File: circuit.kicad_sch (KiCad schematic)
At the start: 9 parts, among them J1 CONN4, U1 LM358, U2 74HC00

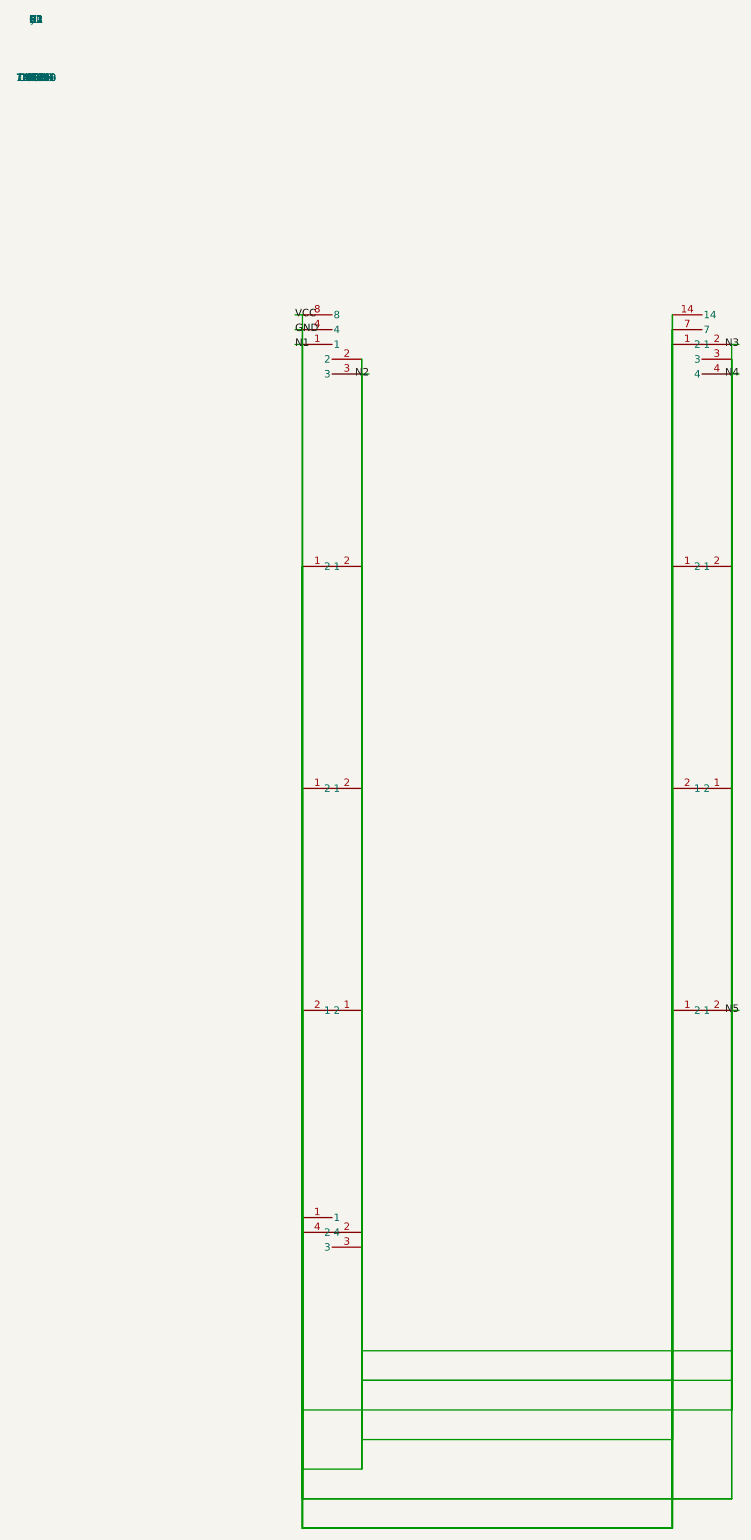
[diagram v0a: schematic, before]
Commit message: fix: v0.5.2 — KiCad pin-transform authority + net-derivation fidelity + schematic best-practice checks
Validation round: live-probed KiCad 10.0.6 itself with a 4-pin symbol
at instance rot 0 and rot 90, all four pin directions. AUTHORITATIVE
transform: a lib pin (px,py) renders at origin + R(-rot)·(px,-py) —
mirror the lib Y, then rotate by MINUS the instance rotation. The
v0.4.2 'mirror-only' inference was rot-0-only evidence; the earlier
mirror-then-rotate-by-+rot double-flipped rot-180 pins onto their
neighbors (found by the decoupling test).

NET DERIVATION FIDELITY (live-verified against kicad-cli's own netlist):
- point-on-segment connection added so labels attach anywhere along a
  wire (midpoint labels previously produced unnamed nets)
- scoped to labels/no-connects only: KiCad connects PINS to wires only
  at wire ENDPOINTS — a wire passing through a pin position is NOT a
  connection (the generated 555's long vertical drops pass near other
  pins; the unscoped test merged every net into one)
- HashMap key type bug in the decoupling check fixed (a &String key vs
  &str lookup silently returned 0 and disabled the check)

SCHEMATIC BEST PRACTICE (per the harness directive):
- missing-decoupling ERC check: an IC power net without a capacitor
  flags with the skill-102 guidance (100nF within 2mm) — the cap
  heuristic now matches the lib type suffix ('Device:C' yes, 'Device:R'
  no — the word 'Device' itself contains a 'C' and false-positived)
- physics-driven placement intent: components ≥0.5W get apart ≥15mm
  separation via the placer's constraint solver

E2E verified on all three fixtures: nets derived correctly (555: VCC/
GND/OUT separate), decoupling fires where caps are absent (555, RF)
and stays silent where present (stress), kicad-cli DRC 0 unconnected +
0 electrical on all three, KiCad reads 7 correct nets from the stress
schematic's exported netlist.

151/151 tests.
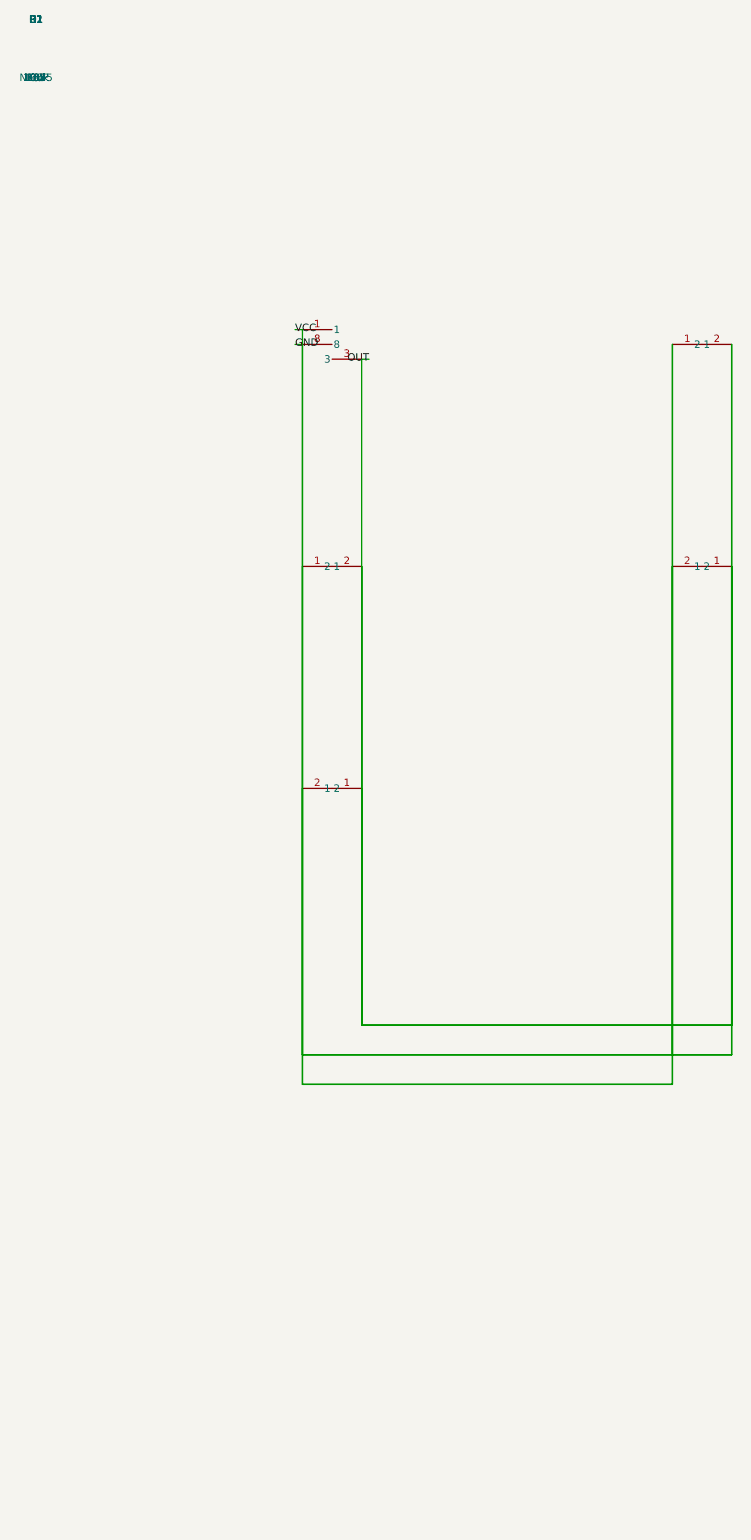
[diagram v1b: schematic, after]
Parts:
- removed C2: 10uF, symbol Device:C
- removed J1: CONN4, symbol Connector:Conn_01x04
- removed R3: 1k, symbol Device:R
- removed U2: 74HC00, symbol Logic:74HC00
- C1: value 100nF -> 10uF
- D1: value 1N4148 -> red; symbol Device:D -> Device:LED
- R2: value 4k7 -> 100k
- U1: value LM358 -> NE555; symbol Amplifier:LM358 -> Timer:NE555
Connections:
- net GND: no longer U1.2, U1.4
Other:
- title: stress test -> 555 LED blinker
- moved on the sheet: C1, D1, R1, R2
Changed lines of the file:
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@@
 (kicad_sch (version 20220904) (generator someda)
-  (title_block (title "stress test"))
-  (wire (pts (xy 45.72 45.72) (xy 45.72 254.00)) (uuid wire_0) )
-  (wire (pts (xy 45.72 254.00) (xy 109.22 254.00)) (uuid wire_1) )
-  (wire (pts (xy 109.22 254.00) (xy 109.22 45.72)) (uuid wire_2) )
-  (wire (pts (xy 109.22 45.72) (xy 109.22 254.00)) (uuid wire_3) )
-  (wire (pts (xy 109.22 254.00) (xy 45.72 254.00)) (uuid wire_4) )
-  (wire (pts (xy 45.72 254.00) (xy 45.72 88.90)) (uuid wire_5) )
-  (wire (pts (xy 45.72 88.90) (xy 45.72 254.00)) (uuid wire_6) )
-  (wire (pts (xy 45.72 254.00) (xy 109.22 254.00)) (uuid wire_7) )
-  (wire (pts (xy 109.22 254.00) (xy 109.22 127.00)) (uuid wire_8) )
-  (wire (pts (xy 109.22 127.00) (xy 109.22 254.00)) (uuid wire_9) )
-  (wire (pts (xy 109.22 254.00) (xy 45.72 254.00)) (uuid wire_10) )
-  (wire (pts (xy 45.72 254.00) (xy 45.72 200.66)) (uuid wire_11) )
-  (wire (pts (xy 45.72 45.72) (xy 44.45 45.72)) (uuid wire_12) )
-  (label "VCC" (at 44.45 45.72 0))
-  (wire (pts (xy 45.72 48.26) (xy 45.72 248.92)) (uuid wire_13) )
-  (wire (pts (xy 45.72 248.92) (xy 109.22 248.92)) (uuid wire_14) )
-  (wire (pts (xy 109.22 248.92) (xy 109.22 48.26)) (uuid wire_15) )
-  (wire (pts (xy 109.22 48.26) (xy 109.22 248.92)) (uuid wire_16) )
-  (wire (pts (xy 109.22 248.92) (xy 119.38 248.92)) (uuid wire_17) )
-  (wire (pts (xy 119.38 248.92) (xy 119.38 127.00)) (uuid wire_18) )
-  (wire (pts (xy 119.38 127.00) (xy 119.38 248.92)) (uuid wire_19) )
-  (wire (pts (xy 119.38 248.92) (xy 45.72 248.92)) (uuid wire_20) )
-  (wire (pts (xy 45.72 248.92) (xy 45.72 165.10)) (uuid wire_21) )
-  (wire (pts (xy 45.72 165.10) (xy 45.72 248.92)) (uuid wire_22) )
-  (wire (pts (xy 45.72 248.92) (xy 45.72 248.92)) (uuid wire_23) )
-  (wire (pts (xy 45.72 248.92) (xy 45.72 203.20)) (uuid wire_24) )
-  (wire (pts (xy 45.72 48.26) (xy 44.45 48.26)) (uuid wire_25) )
-  (label "GND" (at 44.45 48.26 0))
-  (wire (pts (xy 45.72 50.80) (xy 45.72 243.84)) (uuid wire_26) )
-  (wire (pts (xy 45.72 243.84) (xy 55.88 243.84)) (uuid wire_27) )
-  (wire (pts (xy 55.88 243.84) (xy 55.88 53.34)) (uuid wire_28) )
-  (wire (pts (xy 55.88 53.34) (xy 55.88 243.84)) (uuid wire_29) )
-  (wire (pts (xy 55.88 243.84) (xy 55.88 243.84)) (uuid wire_30) )
-  (wire (pts (xy 55.88 243.84) (xy 55.88 88.90)) (uuid wire_31) )
-  (wire (pts (xy 45.72 50.80) (xy 44.45 50.80)) (uuid wire_32) )
-  (label "N1" (at 44.45 50.80 0))
-  (wire (pts (xy 55.88 55.88) (xy 55.88 238.76)) (uuid wire_33) )
-  (wire (pts (xy 55.88 238.76) (xy 109.22 238.76)) (uuid wire_34) )
-  (wire (pts (xy 109.22 238.76) (xy 109.22 88.90)) (uuid wire_35) )
-  (wire (pts (xy 109.22 88.90) (xy 109.22 238.76)) (uuid wire_36) )
-  (wire (pts (xy 109.22 238.76) (xy 109.22 238.76)) (uuid wire_37) )
-  (wire (pts (xy 109.22 238.76) (xy 109.22 50.80)) (uuid wire_38) )
-  (wire (pts (xy 55.88 55.88) (xy 57.15 55.88)) (uuid wire_39) )
-  (label "N2" (at 57.15 55.88 180))
-  (wire (pts (xy 119.38 50.80) (xy 119.38 233.68)) (uuid wire_40) )
-  (wire (pts (xy 119.38 233.68) (xy 119.38 233.68)) (uuid wire_41) )
-  (wire (pts (xy 119.38 233.68) (xy 119.38 53.34)) (uuid wire_42) )
-  (wire (pts (xy 119.38 53.34) (xy 119.38 233.68)) (uuid wire_43) )
-  (wire (pts (xy 119.38 233.68) (xy 119.38 233.68)) (uuid wire_44) )
-  (wire (pts (xy 119.38 233.68) (xy 119.38 88.90)) (uuid wire_45) )
-  (wire (pts (xy 119.38 88.90) (xy 119.38 233.68)) (uuid wire_46) )
-  (wire (pts (xy 119.38 233.68) (xy 45.72 233.68)) (uuid wire_47) )
-  (wire (pts (xy 45.72 233.68) (xy 45.72 127.00)) (uuid wire_48) )
-  (wire (pts (xy 119.38 50.80) (xy 120.65 50.80)) (uuid wire_49) )
-  (label "N3" (at 120.65 50.80 180))
-  (wire (pts (xy 119.38 55.88) (xy 119.38 228.60)) (uuid wire_50) )
-  (wire (pts (xy 119.38 228.60) (xy 55.88 228.60)) (uuid wire_51) )
-  (wire (pts (xy 55.88 228.60) (xy 55.88 165.10)) (uuid wire_52) )
-  (wire (pts (xy 55.88 165.10) (xy 55.88 228.60)) (uuid wire_53) )
-  (wire (pts (xy 55.88 228.60) (xy 109.22 228.60)) (uuid wire_54) )
-  (wire (pts (xy 109.22 228.60) (xy 109.22 165.10)) (uuid wire_55) )
-  (wire (pts (xy 119.38 55.88) (xy 120.65 55.88)) (uuid wire_56) )
-  (label "N4" (at 120.65 55.88 180))
-  (wire (pts (xy 119.38 165.10) (xy 119.38 223.52)) (uuid wire_57) )
-  (wire (pts (xy 119.38 223.52) (xy 55.88 223.52)) (uuid wire_58) )
-  (wire (pts (xy 55.88 223.52) (xy 55.88 127.00)) (uuid wire_59) )
-  (wire (pts (xy 55.88 127.00) (xy 55.88 223.52)) (uuid wire_60) )
-  (wire (pts (xy 55.88 223.52) (xy 55.88 223.52)) (uuid wire_61) )
-  (wire (pts (xy 55.88 223.52) (xy 55.88 203.20)) (uuid wire_62) )
-  (wire (pts (xy 55.88 203.20) (xy 55.88 223.52)) (uuid wire_63) )
-  (wire (pts (xy 55.88 223.52) (xy 55.88 223.52)) (uuid wire_64) )
-  (wire (pts (xy 55.88 223.52) (xy 55.88 205.74)) (uuid wire_65) )
-  (wire (pts (xy 119.38 165.10) (xy 120.65 165.10)) (uuid wire_66) )
-  (label "N5" (at 120.65 165.10 180))
-  (symbol (lib_id "Amplifier:LM358") (at 50.80 50.80 0) (unit 1)
+  (title_block (title "555 LED blinker"))
+  (wire (pts (xy 45.72 48.26) (xy 45.72 177.80)) (uuid wire_0) )
+  (wire (pts (xy 45.72 177.80) (xy 109.22 177.80)) (uuid wire_1) )
+  (wire (pts (xy 109.22 177.80) (xy 109.22 50.80)) (uuid wire_2) )
+  (wire (pts (xy 109.22 50.80) (xy 109.22 177.80)) (uuid wire_3) )
+  (wire (pts (xy 109.22 177.80) (xy 45.72 177.80)) (uuid wire_4) )
+  (wire (pts (xy 45.72 177.80) (xy 45.72 88.90)) (uuid wire_5) )
+  (wire (pts (xy 45.72 48.26) (xy 44.45 48.26)) (uuid wire_6) )
+  (label "VCC" (at 44.45 48.26 0))
+  (wire (pts (xy 45.72 50.80) (xy 45.72 172.72)) (uuid wire_7) )
+  (wire (pts (xy 45.72 172.72) (xy 119.38 172.72)) (uuid wire_8) )
+  (wire (pts (xy 119.38 172.72) (xy 119.38 50.80)) (uuid wire_9) )
+  (wire (pts (xy 119.38 50.80) (xy 119.38 172.72)) (uuid wire_10) )
+  (wire (pts (xy 119.38 172.72) (xy 109.22 172.72)) (uuid wire_11) )
+  (wire (pts (xy 109.22 172.72) (xy 109.22 88.90)) (uuid wire_12) )
+  (wire (pts (xy 109.22 88.90) (xy 109.22 172.72)) (uuid wire_13) )
+  (wire (pts (xy 109.22 172.72) (xy 45.72 172.72)) (uuid wire_14) )
+  (wire (pts (xy 45.72 172.72) (xy 45.72 127.00)) (uuid wire_15) )
+  (wire (pts (xy 45.72 50.80) (xy 44.45 50.80)) (uuid wire_16) )
+  (label "GND" (at 44.45 50.80 0))
+  (wire (pts (xy 55.88 53.34) (xy 55.88 167.64)) (uuid wire_17) )
+  (wire (pts (xy 55.88 167.64) (xy 55.88 167.64)) (uuid wire_18) )
+  (wire (pts (xy 55.88 167.64) (xy 55.88 88.90)) (uuid wire_19) )
+  (wire (pts (xy 55.88 88.90) (xy 55.88 167.64)) (uuid wire_20) )
+  (wire (pts (xy 55.88 167.64) (xy 119.38 167.64)) (uuid wire_21) )
+  (wire (pts (xy 119.38 167.64) (xy 119.38 88.90)) (uuid wire_22) )
+  (wire (pts (xy 119.38 88.90) (xy 119.38 167.64)) (uuid wire_23) )
+  (wire (pts (xy 119.38 167.64) (xy 55.88 167.64)) (uuid wire_24) )
+  (wire (pts (xy 55.88 167.64) (xy 55.88 127.00)) (uuid wire_25) )
+  (wire (pts (xy 55.88 53.34) (xy 57.15 53.34)) (uuid wire_26) )
+  (label "OUT" (at 57.15 53.34 180))
+  (symbol (lib_id "Timer:NE555") (at 50.80 50.80 0) (unit 1)
 (property "Reference" "U1" (at 0 -5 0))
-(property "Value" "LM358" (at 0 5 0))
+(property "Value" "NE555" (at 0 5 0))
   )
-  (symbol (lib_id "Logic:74HC00") (at 114.30 50.80 0) (unit 1)
-(property "Reference" "U2" (at 0 -5 0))
-(property "Value" "74HC00" (at 0 5 0))
-  )
-  (symbol (lib_id "Device:R") (at 50.80 88.90 0) (unit 1)
+  (symbol (lib_id "Device:R") (at 114.30 50.80 0) (unit 1)
 (property "Reference" "R1" (at 0 -5 0))
 (property "Value" "10k" (at 0 5 0))
   )
-  (symbol (lib_id "Device:R") (at 114.30 88.90 0) (unit 1)
+  (symbol (lib_id "Device:R") (at 50.80 88.90 0) (unit 1)
 (property "Reference" "R2" (at 0 -5 0))
-(property "Value" "4k7" (at 0 5 0))
+(property "Value" "100k" (at 0 5 0))
   )
-  (symbol (lib_id "Device:R") (at 50.80 127.00 0) (unit 1)
-(property "Reference" "R3" (at 0 -5 0))
-(property "Value" "1k" (at 0 5 0))
-  )
-  (symbol (lib_id "Device:C") (at 114.30 127.00 0) (unit 1)
+  (symbol (lib_id "Device:C") (at 114.30 88.90 0) (unit 1)
 (property "Reference" "C1" (at 0 -5 0))
-(property "Value" "100nF" (at 0 5 0))
-  )
-  (symbol (lib_id "Device:C") (at 50.80 165.10 0) (unit 1)
-(property "Reference" "C2" (at 0 -5 0))
 (property "Value" "10uF" (at 0 5 0))
   )
-  (symbol (lib_id "Device:D") (at 114.30 165.10 0) (unit 1)
+  (symbol (lib_id "Device:LED") (at 50.80 127.00 0) (unit 1)
 (property "Reference" "D1" (at 0 -5 0))
-(property "Value" "1N4148" (at 0 5 0))
-  )
-  (symbol (lib_id "Connector:Conn_01x04") (at 50.80 203.20 0) (unit 1)
-(property "Reference" "J1" (at 0 -5 0))
-(property "Value" "CONN4" (at 0 5 0))
+(property "Value" "red" (at 0 5 0))
   )
 )
